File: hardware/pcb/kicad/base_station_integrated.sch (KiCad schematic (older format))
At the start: 2 parts, among them P1 CONN_20X2, U1 PAPILIO_TART

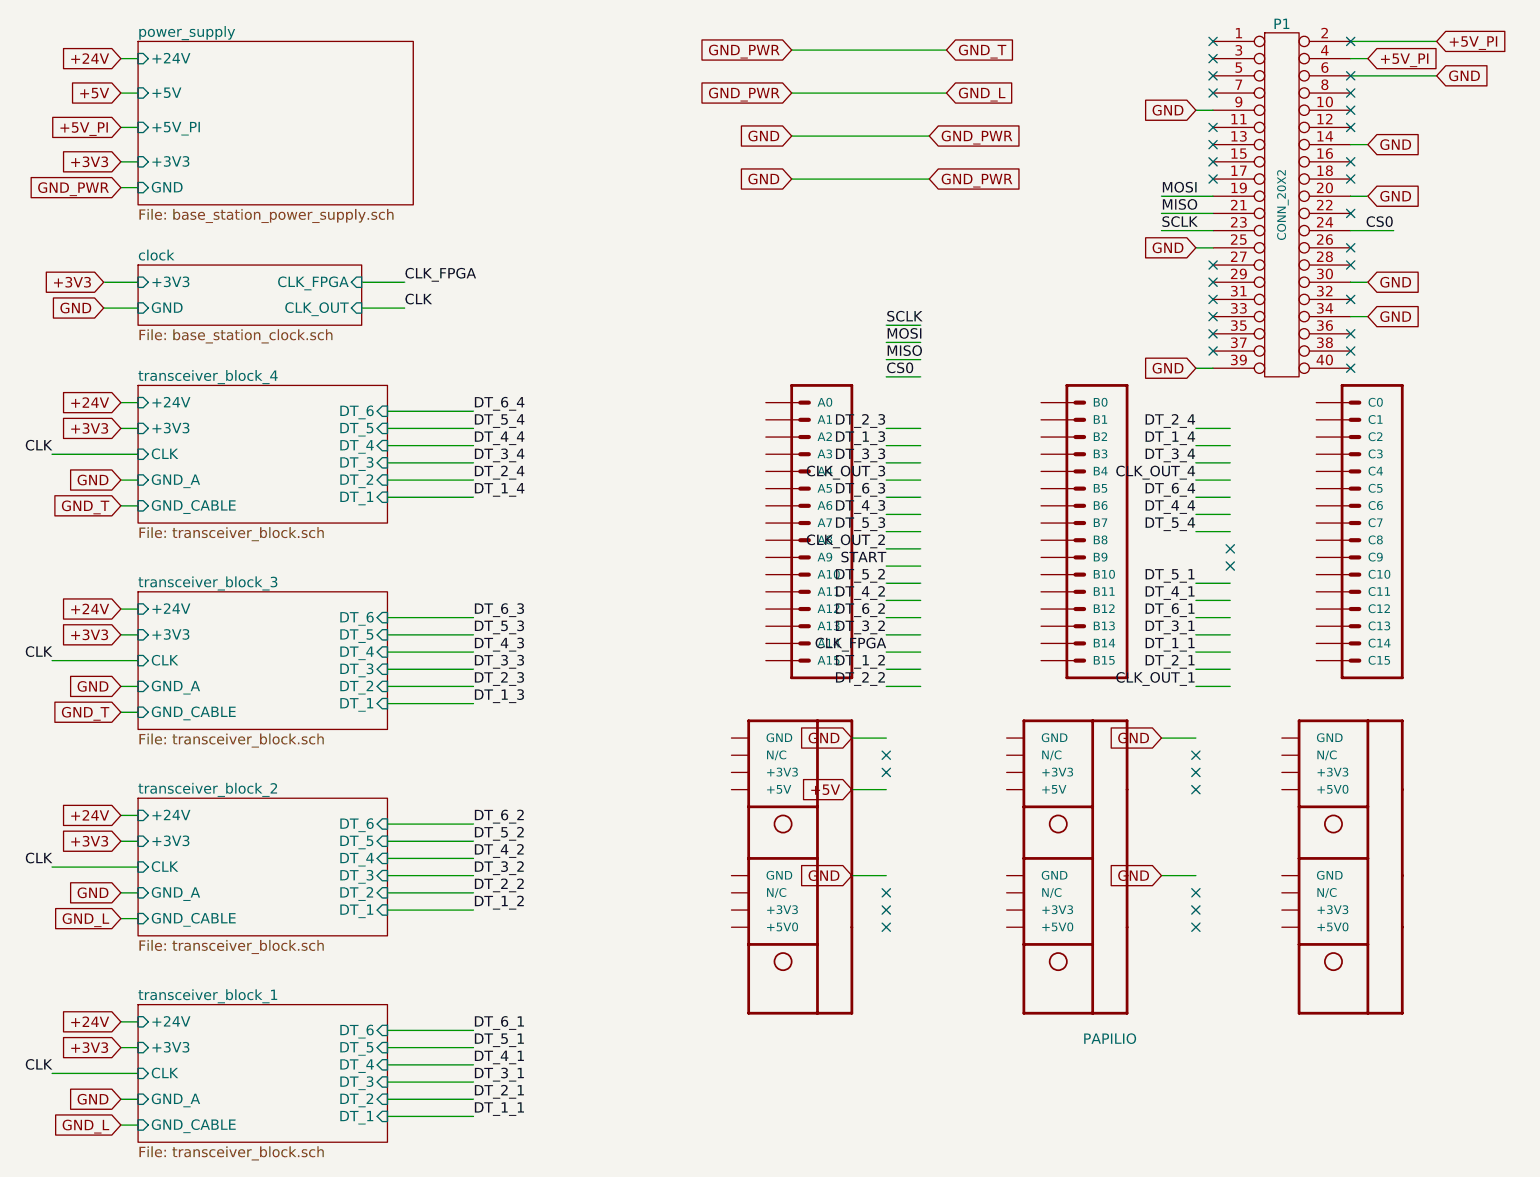
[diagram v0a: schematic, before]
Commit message: Updated silkscreen ready for manufacture
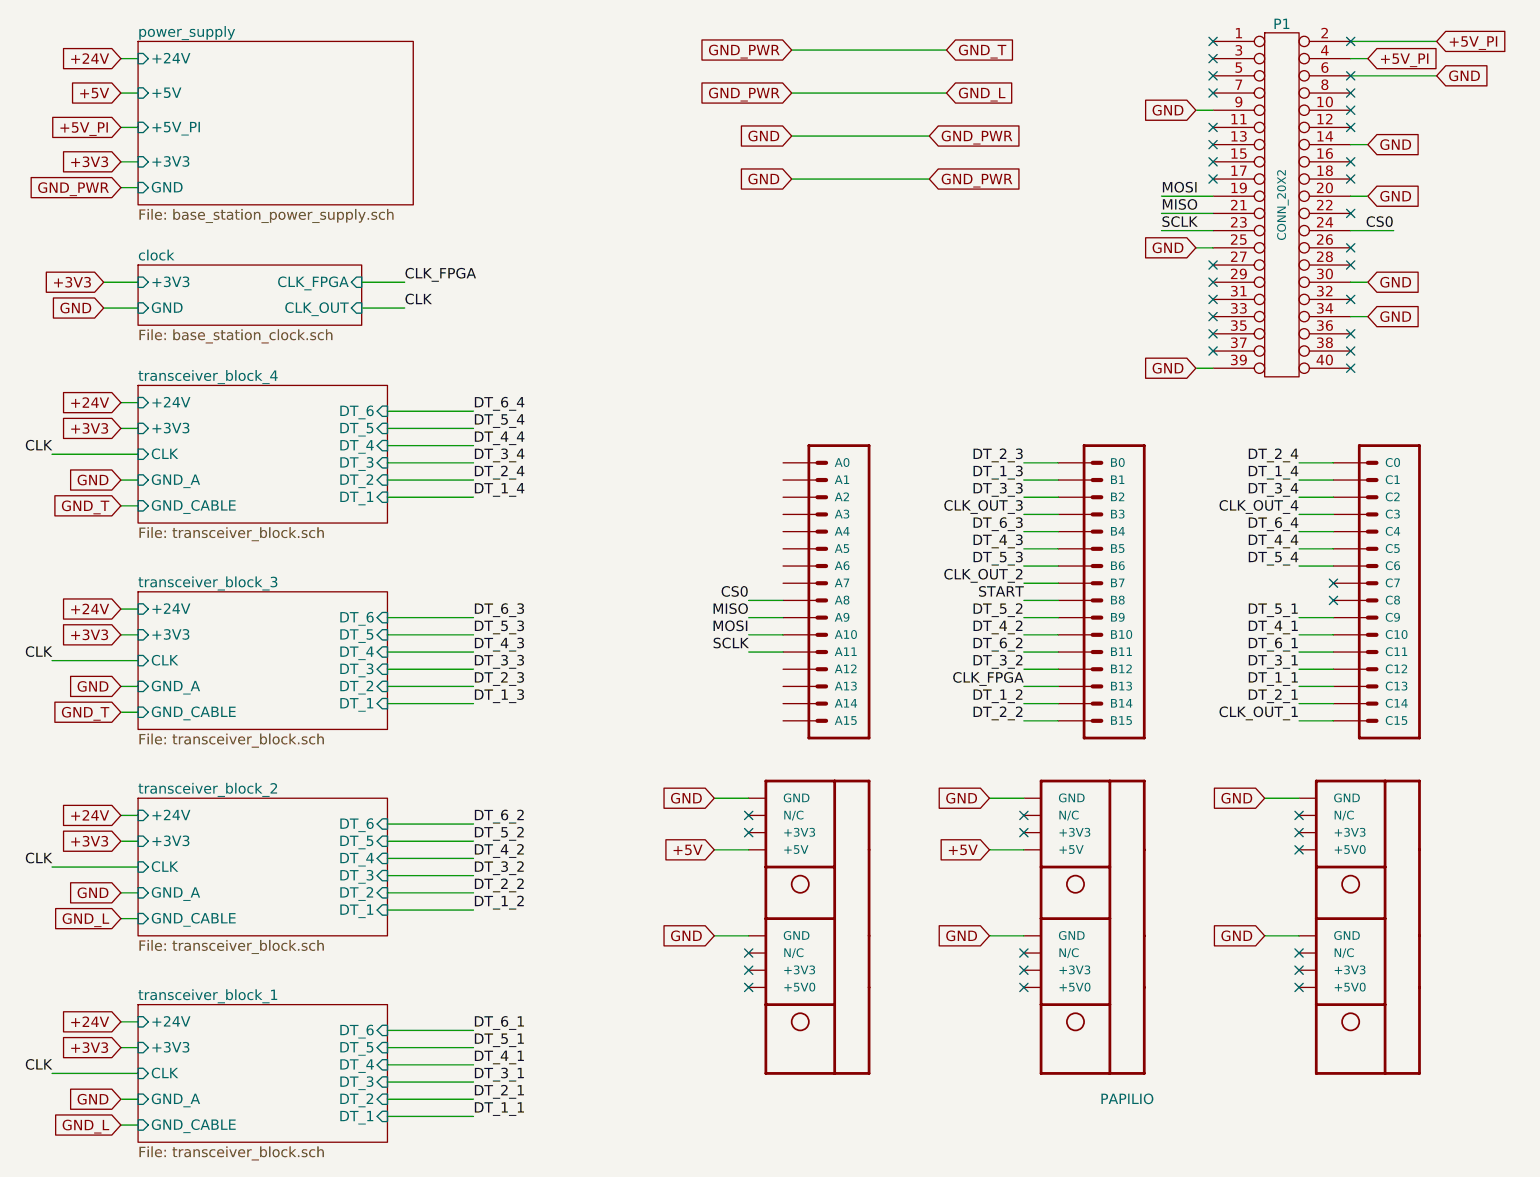
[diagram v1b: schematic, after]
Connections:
- wire segments 110 -> 113
- no-connect marks 41 -> 46
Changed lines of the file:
@@
 Sheet 1 7
 Title ""
-Date "29 oct 2014"
+Date "30 oct 2014"
 Rev ""
 Comp ""
@@
 L PAPILIO_TART U1
 U 1 1 54238645
-P 7850 3800
-F 0 "U1" H 7850 3800 10  0001 C CNN
-F 1 "PAPILIO_TART" H 8650 850 60  0001 C CNN
-F 2 "" H 7850 3800 60  0001 C CNN
-F 3 "" H 7850 3800 60  0001 C CNN
-F 4 "PAPILIO" H 8650 950 60  0000 C CNN "NAME"
-	1    7850 3800
+P 7950 4150
+F 0 "U1" H 7950 4150 10  0001 C CNN
+F 1 "PAPILIO_TART" H 8750 1200 60  0001 C CNN
+F 2 "" H 7950 4150 60  0001 C CNN
+F 3 "" H 7950 4150 60  0001 C CNN
+F 4 "PAPILIO" H 8750 1300 60  0000 C CNN "NAME"
+	1    7950 4150
 	1    0    0    -1
 $EndComp
 Text GLabel 2900 1350 0    60   Input ~ 0
 +5V_PI
-Text Label 7350 2700 0    60   ~ 0
+Text Label 6550 4200 2    60   ~ 0
 MISO
-Text Label 7350 2600 0    60   ~ 0
+Text Label 6550 4300 2    60   ~ 0
 MOSI
-Text Label 7350 2500 0    60   ~ 0
+Text Label 6550 4400 2    60   ~ 0
 SCLK
 Text GLabel 9150 1250 0    60   Input ~ 0
@@
 Text Label 2500 4450 2    60   ~ 0
 CLK
-Text Label 7350 3400 2    60   ~ 0
+Text Label 8150 3600 2    60   ~ 0
 CLK_OUT_3
-Text Label 7350 3200 2    60   ~ 0
+Text Label 8150 3400 2    60   ~ 0
 DT_1_3
 Text Label 4950 4700 0    60   ~ 0
 DT_1_3
-Text Label 7350 3100 2    60   ~ 0
+Text Label 8150 3300 2    60   ~ 0
 DT_2_3
 Text Label 4950 4600 0    60   ~ 0
 DT_2_3
-Text Label 7350 3300 2    60   ~ 0
+Text Label 8150 3500 2    60   ~ 0
 DT_3_3
 Text Label 4950 4500 0    60   ~ 0
 DT_3_3
-Text Label 7350 3600 2    60   ~ 0
+Text Label 8150 3800 2    60   ~ 0
 DT_4_3
 Text Label 4950 4400 0    60   ~ 0
 DT_4_3
-Text Label 7350 3700 2    60   ~ 0
+Text Label 8150 3900 2    60   ~ 0
 DT_5_3
 Text Label 4950 4300 0    60   ~ 0
 DT_5_3
-Text Label 7350 3500 2    60   ~ 0
+Text Label 8150 3700 2    60   ~ 0
 DT_6_3
 Text Label 4950 4200 0    60   ~ 0
@@
 Text GLabel 2900 1700 0    60   Input ~ 0
 GND_PWR
-Text GLabel 8950 5700 0    60   Input ~ 0
-GND
-Text GLabel 8950 4900 0    60   Input ~ 0
-GND
-Text GLabel 7150 5700 0    60   Input ~ 0
-GND
-Text GLabel 7150 5200 0    60   Input ~ 0
+Text GLabel 9550 6050 0    60   Input ~ 0
+GND
+Text GLabel 9550 5250 0    60   Input ~ 0
+GND
+Text GLabel 6350 6050 0    60   Input ~ 0
+GND
+Text GLabel 6350 5550 0    60   Input ~ 0
 +5V
-Text GLabel 7150 4900 0    60   Input ~ 0
-GND
-NoConn ~ 9150 5000
-NoConn ~ 9150 5100
-NoConn ~ 9150 5200
-NoConn ~ 9150 5800
-NoConn ~ 9150 5900
-NoConn ~ 9150 6000
-NoConn ~ 7350 6000
-NoConn ~ 7350 5900
-NoConn ~ 7350 5800
-NoConn ~ 7350 5100
-NoConn ~ 7350 5000
-Text Label 7350 4400 2    60   ~ 0
+Text GLabel 6350 5250 0    60   Input ~ 0
+GND
+NoConn ~ 9750 5350
+NoConn ~ 9750 5450
+NoConn ~ 9750 5550
+NoConn ~ 9750 6150
+NoConn ~ 9750 6250
+NoConn ~ 9750 6350
+NoConn ~ 6550 6350
+NoConn ~ 6550 6250
+NoConn ~ 6550 6150
+NoConn ~ 6550 5450
+NoConn ~ 6550 5350
+Text Label 8150 4600 2    60   ~ 0
 CLK_FPGA
-NoConn ~ 9350 3900
-NoConn ~ 9350 3800
-Text Label 9150 4000 2    60   ~ 0
+NoConn ~ 9950 4100
+NoConn ~ 9950 4000
+Text Label 9750 4200 2    60   ~ 0
 DT_5_1
-Text Label 9150 4100 2    60   ~ 0
+Text Label 9750 4300 2    60   ~ 0
 DT_4_1
-Text Label 9150 4200 2    60   ~ 0
+Text Label 9750 4400 2    60   ~ 0
 DT_6_1
-Text Label 9150 4300 2    60   ~ 0
+Text Label 9750 4500 2    60   ~ 0
 DT_3_1
-Text Label 9150 4400 2    60   ~ 0
+Text Label 9750 4600 2    60   ~ 0
 DT_1_1
-Text Label 9150 4500 2    60   ~ 0
+Text Label 9750 4700 2    60   ~ 0
 DT_2_1
-Text Label 9150 4600 2    60   ~ 0
+Text Label 9750 4800 2    60   ~ 0
 CLK_OUT_1
-Text Label 9150 3700 2    60   ~ 0
+Text Label 9750 3900 2    60   ~ 0
 DT_5_4
-Text Label 9150 3600 2    60   ~ 0
+Text Label 9750 3800 2    60   ~ 0
 DT_4_4
-Text Label 9150 3500 2    60   ~ 0
+Text Label 9750 3700 2    60   ~ 0
 DT_6_4
-Text Label 9150 3400 2    60   ~ 0
+Text Label 9750 3600 2    60   ~ 0
 CLK_OUT_4
-Text Label 9150 3300 2    60   ~ 0
+Text Label 9750 3500 2    60   ~ 0
 DT_3_4
-Text Label 9150 3200 2    60   ~ 0
+Text Label 9750 3400 2    60   ~ 0
 DT_1_4
-Text Label 9150 3100 2    60   ~ 0
+Text Label 9750 3300 2    60   ~ 0
 DT_2_4
-Text Label 7350 4600 2    60   ~ 0
+Text Label 8150 4800 2    60   ~ 0
 DT_2_2
-Text Label 7350 4500 2    60   ~ 0
+Text Label 8150 4700 2    60   ~ 0
 DT_1_2
-Text Label 7350 4300 2    60   ~ 0
+Text Label 8150 4500 2    60   ~ 0
 DT_3_2
-Text Label 7350 4200 2    60   ~ 0
+Text Label 8150 4400 2    60   ~ 0
 DT_6_2
-Text Label 7350 4100 2    60   ~ 0
+Text Label 8150 4300 2    60   ~ 0
 DT_4_2
-Text Label 7350 4000 2    60   ~ 0
+Text Label 8150 4200 2    60   ~ 0
 DT_5_2
-Text Label 7350 3900 2    60   ~ 0
+Text Label 8150 4100 2    60   ~ 0
 START
-Text Label 7350 3800 2    60   ~ 0
+Text Label 8150 4000 2    60   ~ 0
 CLK_OUT_2
 Text Label 4950 3500 0    60   ~ 0
@@
 Text Label 4950 3000 0    60   ~ 0
 DT_6_4
-Text Label 7350 2800 0    60   ~ 0
+Text Label 6550 4100 2    60   ~ 0
 CS0
 Text Label 10300 1950 2    60   ~ 0
@@
 	2900 1350 3000 1350
 Wire Wire Line
-	7550 2700 7350 2700
-Wire Wire Line
-	7550 2500 7350 2500
+	6750 4200 6550 4200
+Wire Wire Line
+	6750 4400 6550 4400
 Wire Wire Line
 	10050 1750 10150 1750
@@
 	2900 4150 3000 4150
 Wire Wire Line
-	7550 3600 7350 3600
-Wire Wire Line
-	7550 3400 7350 3400
-Wire Wire Line
-	7550 3200 7350 3200
+	8350 3800 8150 3800
+Wire Wire Line
+	8350 3600 8150 3600
+Wire Wire Line
+	8350 3400 8150 3400
 Wire Wire Line
 	3000 2250 2800 2250
@@
 	2900 950  3000 950
 Wire Wire Line
-	7350 5700 7150 5700
-Wire Wire Line
-	7350 4900 7150 4900
-Wire Wire Line
-	9150 5700 8950 5700
-Wire Wire Line
-	9150 4900 8950 4900
-Wire Wire Line
-	9350 4500 9150 4500
-Wire Wire Line
-	9350 4300 9150 4300
-Wire Wire Line
-	9350 4100 9150 4100
-Wire Wire Line
-	9350 3700 9150 3700
-Wire Wire Line
-	9350 3500 9150 3500
-Wire Wire Line
-	9350 3300 9150 3300
-Wire Wire Line
-	9350 3100 9150 3100
-Wire Wire Line
-	7550 4500 7350 4500
-Wire Wire Line
-	7550 4300 7350 4300
-Wire Wire Line
-	7550 4100 7350 4100
-Wire Wire Line
-	7550 3900 7350 3900
+	6550 6050 6350 6050
+Wire Wire Line
+	6550 5250 6350 5250
+Wire Wire Line
+	9750 6050 9550 6050
+Wire Wire Line
+	9750 5250 9550 5250
+Wire Wire Line
+	9950 4700 9750 4700
+Wire Wire Line
+	9950 4500 9750 4500
+Wire Wire Line
+	9950 4300 9750 4300
+Wire Wire Line
+	9950 3900 9750 3900
+Wire Wire Line
+	9950 3700 9750 3700
+Wire Wire Line
+	9950 3500 9750 3500
+Wire Wire Line
+	9950 3300 9750 3300
+Wire Wire Line
+	8350 4700 8150 4700
+Wire Wire Line
+	8350 4500 8150 4500
+Wire Wire Line
+	8350 4300 8150 4300
+Wire Wire Line
+	8350 4100 8150 4100
 Wire Wire Line
 	4450 3400 4950 3400
@@
 	4450 3500 4950 3500
 Wire Wire Line
-	7550 3800 7350 3800
-Wire Wire Line
-	7550 4000 7350 4000
-Wire Wire Line
-	7550 4200 7350 4200
-Wire Wire Line
-	7550 4400 7350 4400
-Wire Wire Line
-	7550 4600 7350 4600
-Wire Wire Line
-	9350 3200 9150 3200
-Wire Wire Line
-	9350 3400 9150 3400
-Wire Wire Line
-	9350 3600 9150 3600
-Wire Wire Line
-	9350 4000 9150 4000
-Wire Wire Line
-	9350 4200 9150 4200
-Wire Wire Line
-	9350 4400 9150 4400
-Wire Wire Line
-	9350 4600 9150 4600
-Wire Wire Line
-	7350 5200 7150 5200
+	8350 4000 8150 4000
+Wire Wire Line
+	8350 4200 8150 4200
+Wire Wire Line
+	8350 4400 8150 4400
+Wire Wire Line
+	8350 4600 8150 4600
+Wire Wire Line
+	8350 4800 8150 4800
+Wire Wire Line
+	9950 3400 9750 3400
+Wire Wire Line
+	9950 3600 9750 3600
+Wire Wire Line
+	9950 3800 9750 3800
+Wire Wire Line
+	9950 4200 9750 4200
+Wire Wire Line
+	9950 4400 9750 4400
+Wire Wire Line
+	9950 4600 9750 4600
+Wire Wire Line
+	9950 4800 9750 4800
+Wire Wire Line
+	6550 5550 6350 5550
 Wire Wire Line
 	2900 1550 3000 1550
@@
 	2900 7000 3000 7000
 Wire Wire Line
-	7550 3100 7350 3100
-Wire Wire Line
-	7550 3300 7350 3300
-Wire Wire Line
-	7550 3500 7350 3500
-Wire Wire Line
-	7550 3700 7350 3700
+	8350 3300 8150 3300
+Wire Wire Line
+	8350 3500 8150 3500
+Wire Wire Line
+	8350 3700 8150 3700
+Wire Wire Line
+	8350 3900 8150 3900
 Wire Wire Line
 	2900 4300 3000 4300
@@
 	9250 1250 9150 1250
 Wire Wire Line
-	7550 2600 7350 2600
-Wire Wire Line
-	7550 2800 7350 2800
+	6750 4300 6550 4300
+Wire Wire Line
+	6750 4100 6550 4100
 Wire Wire Line
 	10050 1950 10300 1950
@@
 Wire Wire Line
 	9150 2750 9250 2750
+Text GLabel 7950 6050 0    60   Input ~ 0
+GND
+NoConn ~ 8150 6350
+NoConn ~ 8150 6250
+NoConn ~ 8150 6150
+Wire Wire Line
+	8150 6050 7950 6050
+Text GLabel 7950 5550 0    60   Input ~ 0
++5V
+Text GLabel 7950 5250 0    60   Input ~ 0
+GND
+NoConn ~ 8150 5450
+NoConn ~ 8150 5350
+Wire Wire Line
+	8150 5250 7950 5250
+Wire Wire Line
+	8150 5550 7950 5550
 $EndSCHEMATC
